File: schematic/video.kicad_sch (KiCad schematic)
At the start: 26 parts

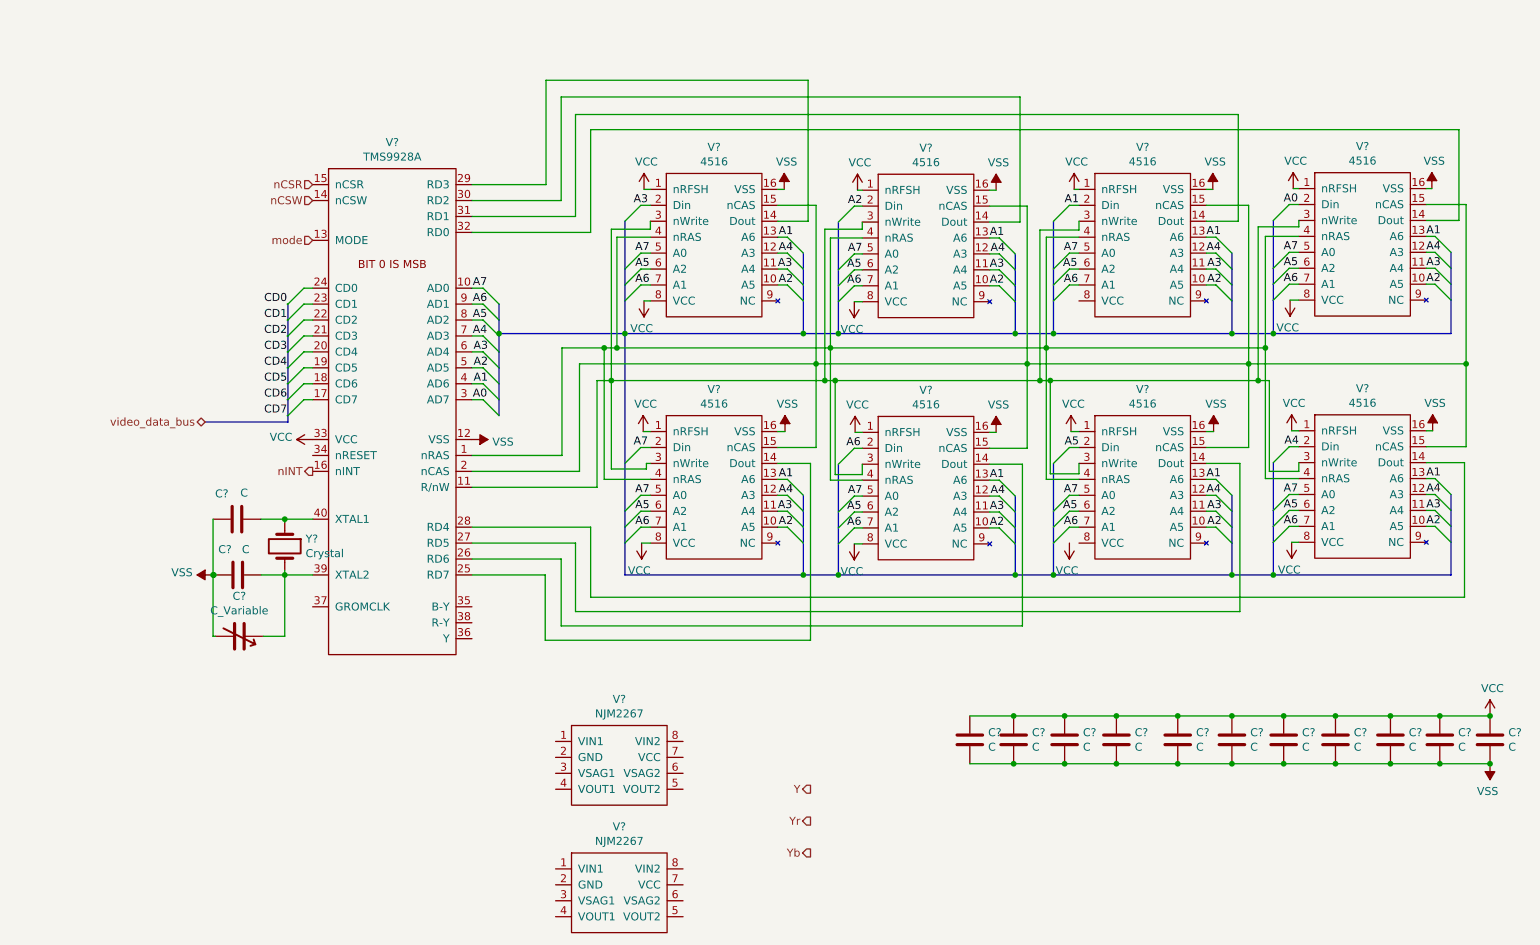
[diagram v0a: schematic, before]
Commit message: revised schematic into sheets for easier design. Looks much better.
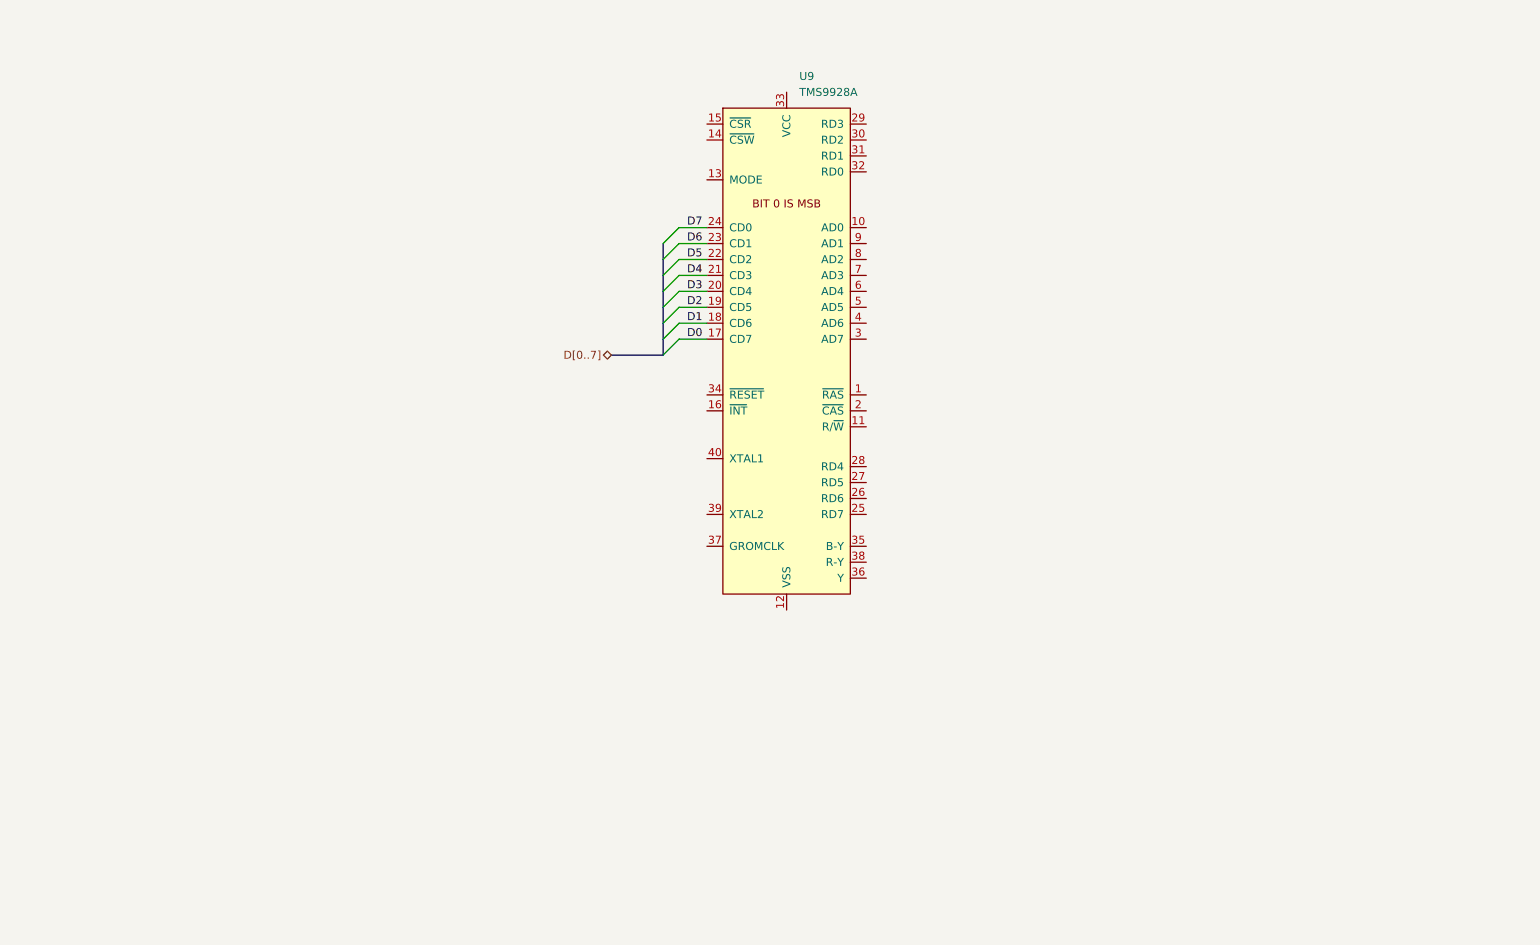
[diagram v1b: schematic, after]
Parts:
- removed C? (x13): C, symbol Device:C
- removed C?: C_Variable, symbol Device:C_Variable
- removed V?: TMS9928A, symbol VINTAGE_PC_VIDEO:TMS9928A
- removed V? (x8): 4516, symbol VINTAGE_PC_VIDEO:4516
- removed V? (x2): NJM2267, symbol VINTAGE_PC_VIDEO:NJM2267
- removed Y?: Crystal, symbol Device:Crystal
- added U9: TMS9928A, symbol VINTAGE_PC_VIDEO:TMS9928A
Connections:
- new net D0: U9.17 (CD7)
- new net D1: U9.18 (CD6)
- new net D2: U9.19 (CD5)
- new net D3: U9.20 (CD4)
- new net D4: U9.21 (CD3)
- new net D5: U9.22 (CD2)
- new net D6: U9.23 (CD1)
- new net D7: U9.24 (CD0)

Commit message: worked on the z80 trace up to and including pin 15.
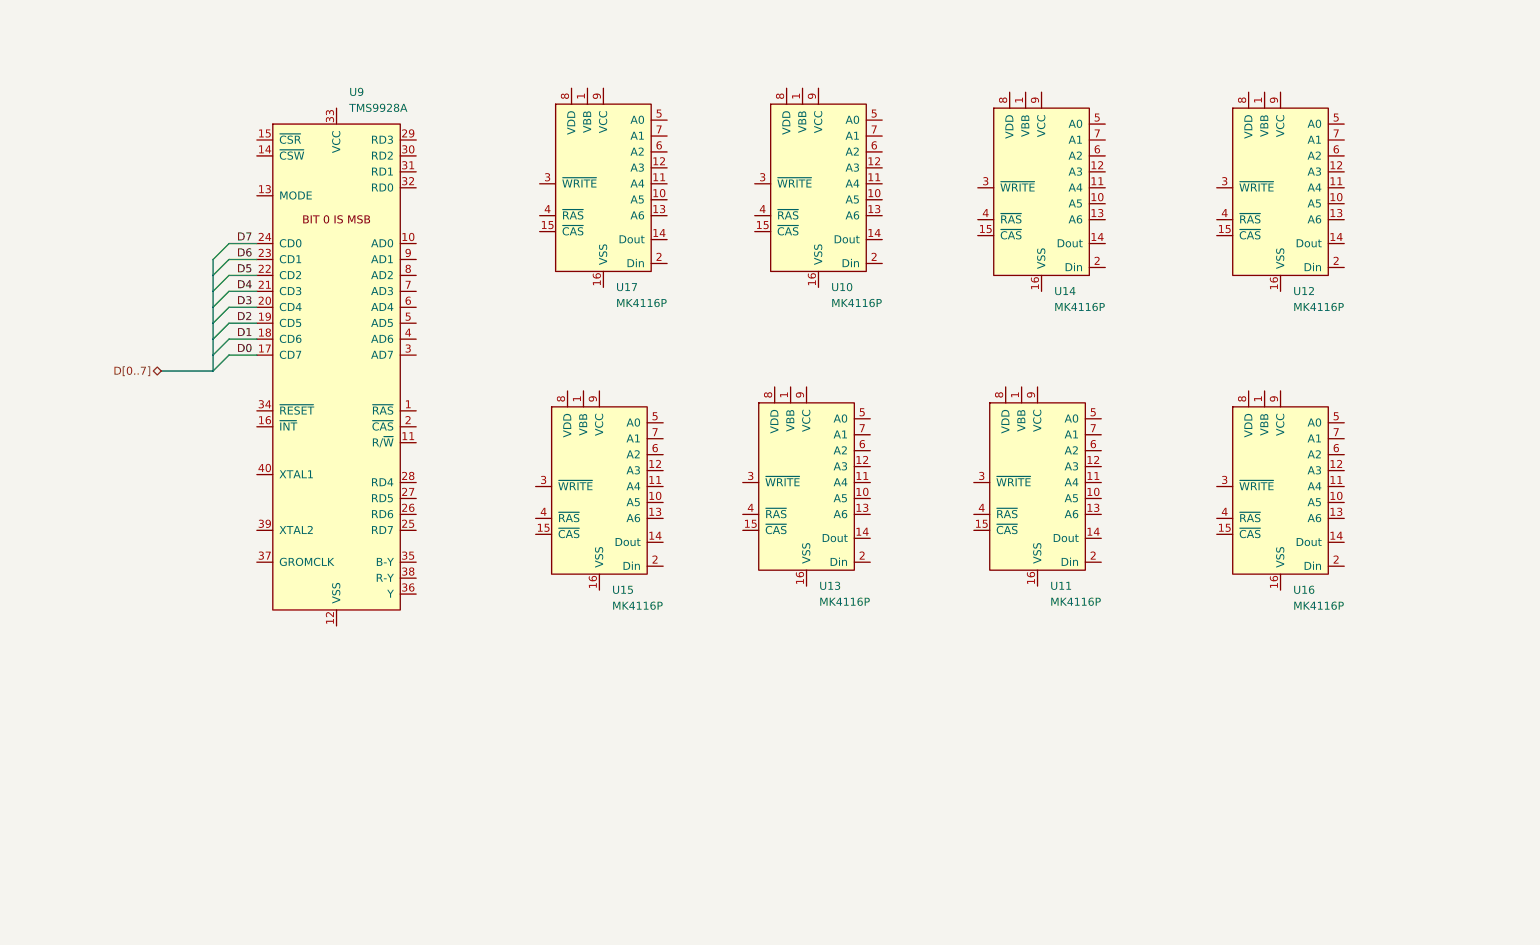
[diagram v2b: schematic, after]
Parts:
- added U10, U11, U12, U13, U14, U15, U16, U17: MK4116P, symbol Vintage_PC_RAM:MK4116P
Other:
- moved on the sheet: U9

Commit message: changed all vintage library names to better represent future ideas. Removed parts not needed... for now. Updated schmematic symbols.
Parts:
- U10, U11, U12, U13, U14, U15, U16, U17: symbol Vintage_PC_RAM:MK4116P -> Vintage_RAM:MK4116P
- U9: symbol VINTAGE_PC_VIDEO:TMS9928A -> Vintage_VDP:TMS9928A
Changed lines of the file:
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@@
     (effects (font (size 1.27 1.27)) (justify right))
   )
-  (symbol (lib_id "Vintage_PC_RAM:MK4116P") (at 178.435 93.345 0) (unit 1)
+  (symbol (lib_id "Vintage_RAM:MK4116P") (at 178.435 93.345 0) (unit 1)
     (in_bom yes) (on_board yes) (fields_autoplaced)
     (property "Reference" "U11" (id 0) (at 180.4544 118.745 0)
@@
     (pin "9")
   )
-  (symbol (lib_id "Vintage_PC_RAM:MK4116P") (at 217.17 93.98 0) (unit 1)
+  (symbol (lib_id "Vintage_RAM:MK4116P") (at 217.17 93.98 0) (unit 1)
     (in_bom yes) (on_board yes) (fields_autoplaced)
     (property "Reference" "U16" (id 0) (at 219.1894 119.38 0)
@@
     (pin "9")
   )
-  (symbol (lib_id "Vintage_PC_RAM:MK4116P") (at 141.605 93.345 0) (unit 1)
+  (symbol (lib_id "Vintage_RAM:MK4116P") (at 141.605 93.345 0) (unit 1)
     (in_bom yes) (on_board yes) (fields_autoplaced)
     (property "Reference" "U13" (id 0) (at 143.6244 118.745 0)
@@
     (pin "9")
   )
-  (symbol (lib_id "Vintage_PC_RAM:MK4116P") (at 109.22 45.72 0) (unit 1)
+  (symbol (lib_id "Vintage_RAM:MK4116P") (at 109.22 45.72 0) (unit 1)
     (in_bom yes) (on_board yes) (fields_autoplaced)
     (property "Reference" "U17" (id 0) (at 111.2394 71.12 0)
@@
     (pin "9")
   )
-  (symbol (lib_id "VINTAGE_PC_VIDEO:TMS9928A") (at 66.675 52.705 0) (unit 1)
+  (symbol (lib_id "Vintage_VDP:TMS9928A") (at 66.675 52.705 0) (unit 1)
     (in_bom yes) (on_board yes) (fields_autoplaced)
     (property "Reference" "U9" (id 0) (at 68.6944 40.005 0)
@@
     (pin "9")
   )
-  (symbol (lib_id "Vintage_PC_RAM:MK4116P") (at 108.585 93.98 0) (unit 1)
+  (symbol (lib_id "Vintage_RAM:MK4116P") (at 108.585 93.98 0) (unit 1)
     (in_bom yes) (on_board yes) (fields_autoplaced)
     (property "Reference" "U15" (id 0) (at 110.6044 119.38 0)
@@
     (pin "9")
   )
-  (symbol (lib_id "Vintage_PC_RAM:MK4116P") (at 179.07 46.355 0) (unit 1)
+  (symbol (lib_id "Vintage_RAM:MK4116P") (at 179.07 46.355 0) (unit 1)
     (in_bom yes) (on_board yes) (fields_autoplaced)
     (property "Reference" "U14" (id 0) (at 181.0894 71.755 0)
@@
     (pin "9")
   )
-  (symbol (lib_id "Vintage_PC_RAM:MK4116P") (at 217.17 46.355 0) (unit 1)
+  (symbol (lib_id "Vintage_RAM:MK4116P") (at 217.17 46.355 0) (unit 1)
     (in_bom yes) (on_board yes) (fields_autoplaced)
     (property "Reference" "U12" (id 0) (at 219.1894 71.755 0)
@@
     (pin "9")
   )
-  (symbol (lib_id "Vintage_PC_RAM:MK4116P") (at 143.51 45.72 0) (unit 1)
+  (symbol (lib_id "Vintage_RAM:MK4116P") (at 143.51 45.72 0) (unit 1)
     (in_bom yes) (on_board yes) (fields_autoplaced)
     (property "Reference" "U10" (id 0) (at 145.5294 71.12 0)

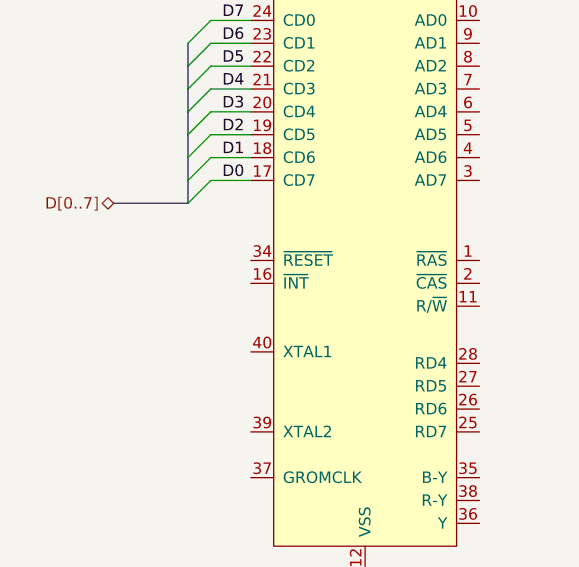
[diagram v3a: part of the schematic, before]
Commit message: Up to pin 29 on z80 done. Address 0 to 10 left. Only tracing to its end point for the most part. Each chip gets traced chip to chip in this manned
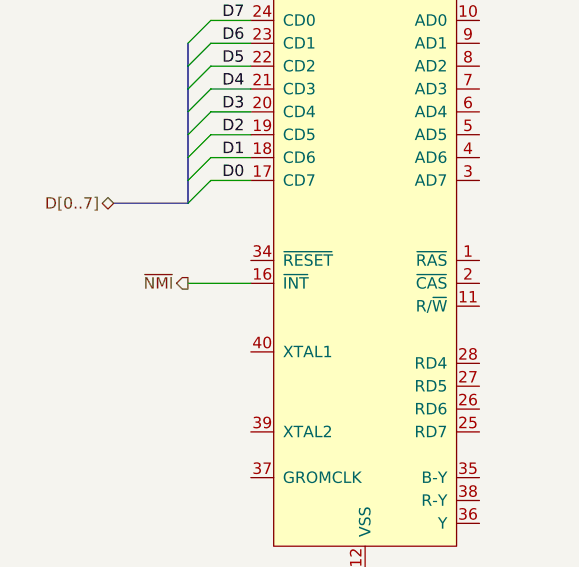
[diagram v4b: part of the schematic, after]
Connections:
- net ~{NMI}: now reaches U9.16 (~{INT})
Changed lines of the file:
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@@
+    (stroke (width 0) (type default) (color 0 0 0 0))
+  )
+  (wire (pts (xy 46.99 93.345) (xy 53.975 93.345))
     (stroke (width 0) (type default) (color 0 0 0 0))
   )
@@
     (effects (font (size 1.27 1.27)) (justify right))
   )
+  (hierarchical_label "~{NMI}" (shape output) (at 46.99 93.345 180)
+    (effects (font (size 1.27 1.27)) (justify right))
+  )

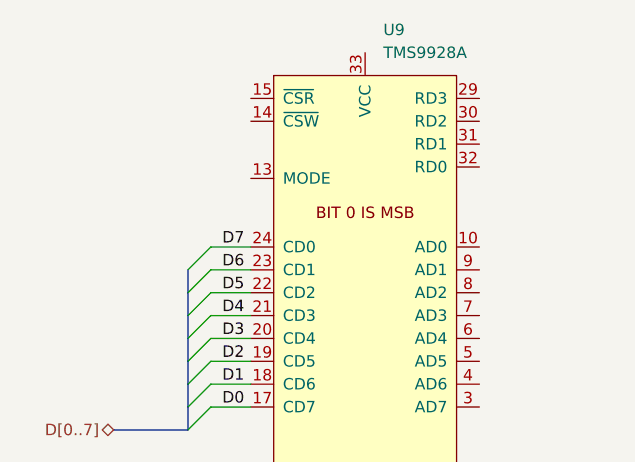
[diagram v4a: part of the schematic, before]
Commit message: completed Z80 trace of PCB. off to a good start.
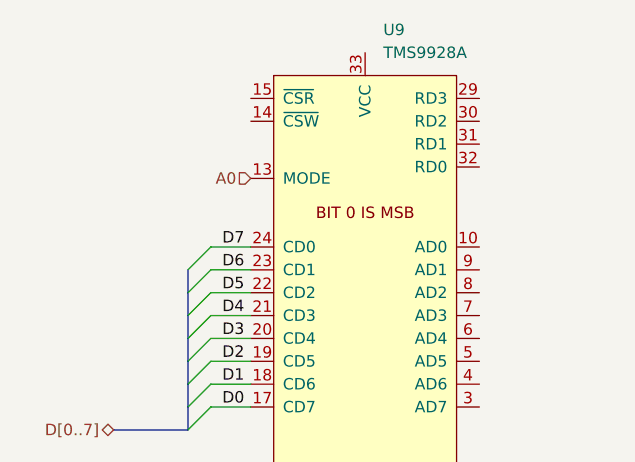
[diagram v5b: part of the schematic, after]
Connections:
- net A0: now reaches U9.13 (MODE)
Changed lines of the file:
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@@
+    (effects (font (size 1.27 1.27)) (justify right))
+  )
+  (hierarchical_label "A0" (shape input) (at 53.975 56.515 180)
     (effects (font (size 1.27 1.27)) (justify right))
   )
